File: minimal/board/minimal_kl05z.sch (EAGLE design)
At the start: 28 parts, among them U1 LPC810M021FN8FP-DIL08, U2 LPC810M021FN8FP-DIL08, U3 LPC810M021FN8FP-DIL08

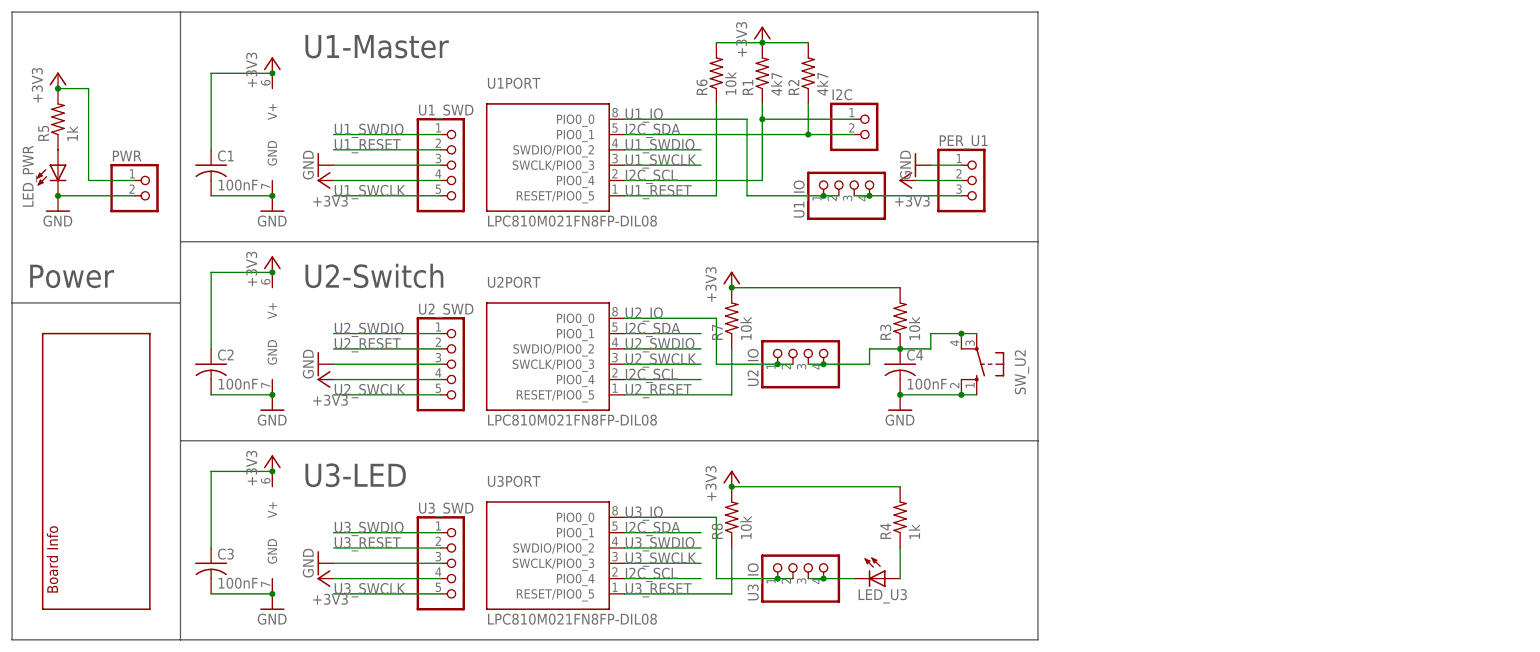
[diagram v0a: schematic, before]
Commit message: Adding all boards for minimal and carrier board with MKL05Z32
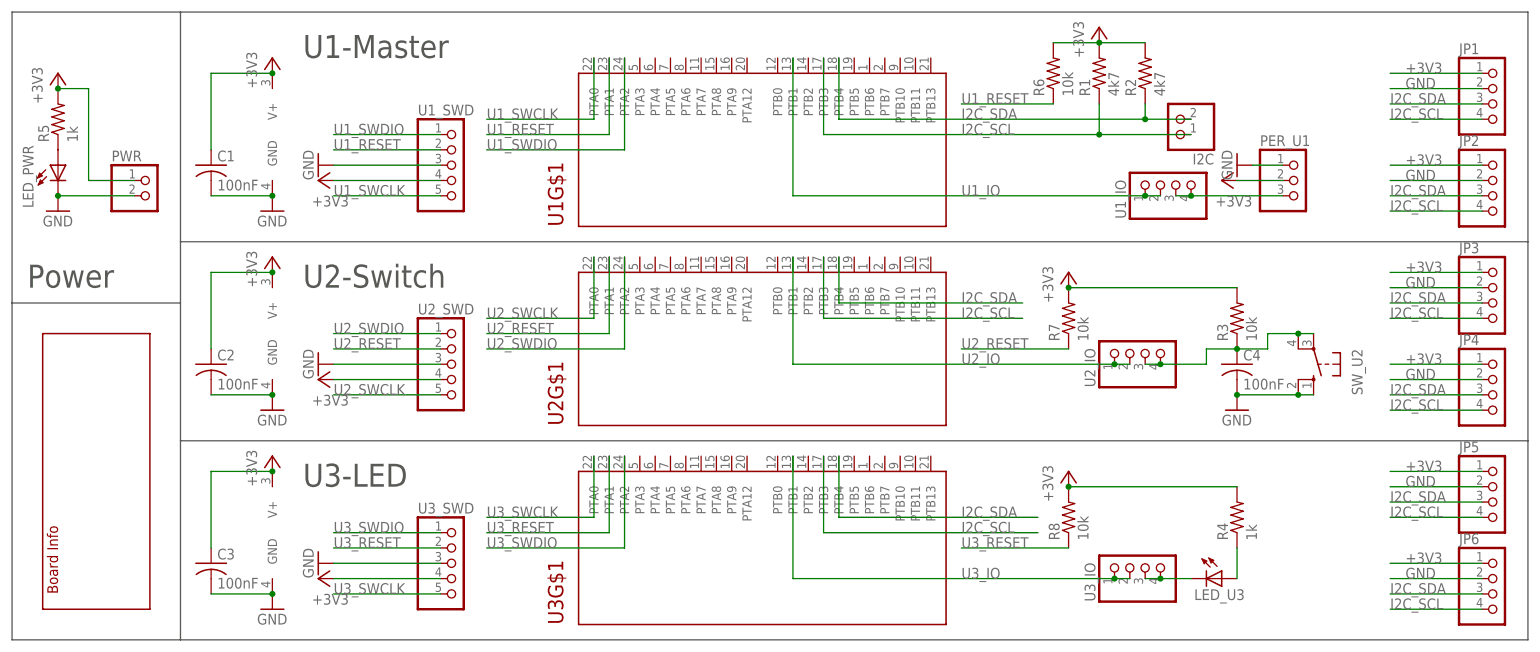
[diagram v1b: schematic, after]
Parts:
- added JP1, JP2, JP3, JP4, JP5, JP6: (no value), pinhead:PINHD-1X4
- U$1: DATE May 29, 2015 -> Jul 7, 2015; DESIGN MinimalModRob -> MinimalKL05Z
- U1, U2, U3: value LPC810M021FN8FP-DIL08 -> MKL05Z32VFK4-DIP; device modular_robotics:LPC810M021FN8FP-DIL08 -> modular_robotics:MKL05Z32VFK4-DIP
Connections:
- net +3V3: now also JP1.1, JP2.1, JP3.1, JP4.1, JP5.1, JP6.1, U1G$2.V+, U2G$2.V+, U3G$2.V+; no longer U1PWR.V+, U2PWR.V+, U3PWR.V+
- net GND: now also JP1.2, JP2.2, JP3.2, JP4.2, JP5.2, JP6.2, U1G$2.GND, U2G$2.GND, U3G$2.GND; no longer U1PWR.GND, U2PWR.GND, U3PWR.GND
- net I2C_SCL: now also JP1.4, JP2.4, JP3.4, JP4.4, JP5.4, JP6.4, U1G$1.PTB3, U2G$1.PTB3, U3G$1.PTB3; no longer U1PORT.PIO0_4, U2PORT.PIO0_4, U3PORT.PIO0_4
- net I2C_SDA: now also JP1.3, JP2.3, JP3.3, JP4.3, JP5.3, JP6.3, U1G$1.PTB4, U2G$1.PTB4, U3G$1.PTB4; no longer U1PORT.PIO0_1, U2PORT.PIO0_1, U3PORT.PIO0_1
- net U1_IO: now also U1G$1.PTB1; no longer U1PORT.PIO0_0
- net U1_RESET: now also U1G$1.PTA1; no longer U1PORT.RESET/PIO0_5
- net U1_SWCLK: now also U1G$1.PTA0; no longer U1PORT.SWCLK/PIO0_3
- net U1_SWDIO: now also U1G$1.PTA2; no longer U1PORT.SWDIO/PIO0_2
- net U2_IO: now also U2G$1.PTB1; no longer U2PORT.PIO0_0
- net U2_RESET: now also U2G$1.PTA1; no longer U2PORT.RESET/PIO0_5
- net U2_SWCLK: now also U2G$1.PTA0; no longer U2PORT.SWCLK/PIO0_3
- net U2_SWDIO: now also U2G$1.PTA2; no longer U2PORT.SWDIO/PIO0_2
- net U3_IO: now also U3G$1.PTB1; no longer U3PORT.PIO0_0
- net U3_RESET: now also U3G$1.PTA1; no longer U3PORT.RESET/PIO0_5
- net U3_SWCLK: now also U3G$1.PTA0; no longer U3PORT.SWCLK/PIO0_3
- net U3_SWDIO: now also U3G$1.PTA2; no longer U3PORT.SWDIO/PIO0_2
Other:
- moved on the sheet: C4, I2C, LED_U3, PER_U1, R1, R2, R3, R4, R6, R7, R8, SW_U2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
